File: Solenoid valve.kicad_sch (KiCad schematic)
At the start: 22 parts, among them J1 Conn_01x02, J2 Conn_01x02, J3 Conn_01x02, J4 Conn_01x02, Q1 S8050, Q2 S8050, U1 BTS443P

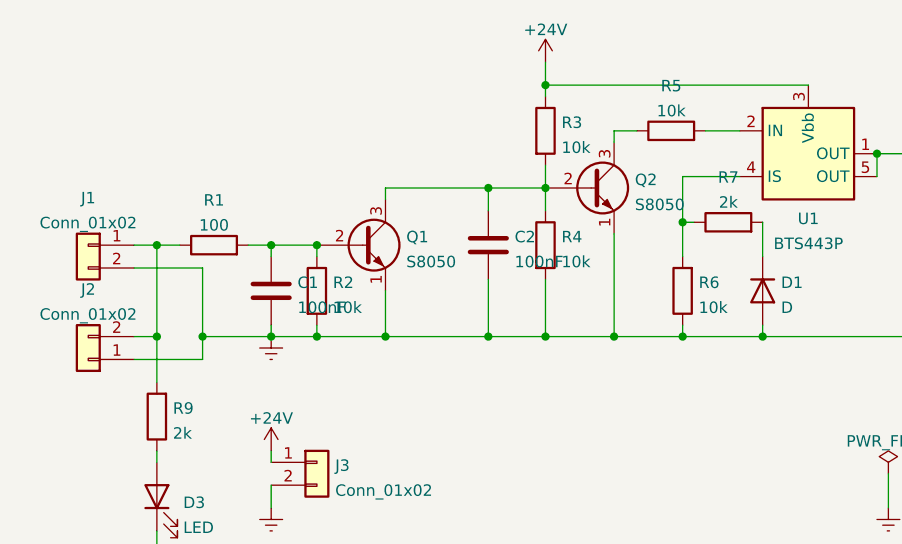
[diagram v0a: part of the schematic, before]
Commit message: Change some routings and S8050's footprint
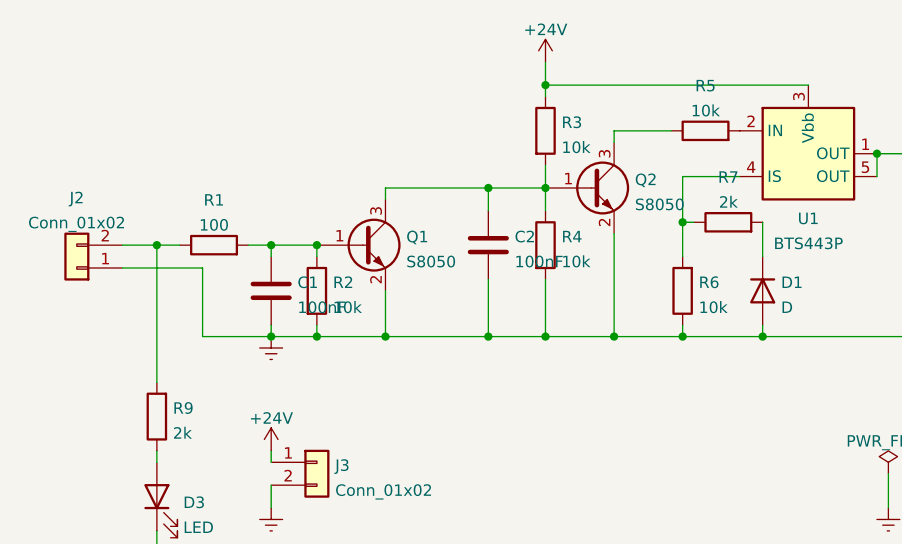
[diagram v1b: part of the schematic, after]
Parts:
- removed J1: Conn_01x02, Connector_AMASS:AMASS_XT30UPB-M_1x02_P5.0mm_Vertical, symbol Connector_Generic:Conn_01x02
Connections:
- net Earth: now also Q1.2 (E), Q2.2 (E); no longer Q1.1 (E), Q2.1 (E)
- net at C1.1, R1.2, R2.1: now also Q1.1 (B); no longer Q1.2 (B)
- net at C2.1, Q1.3 (C), R3.2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: now also Q2.1 (B); no longer Q2.2 (B)
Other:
- moved on the sheet: J2, R5
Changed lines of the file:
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@@
   (junction (at 181.61 66.04) (diameter 0) (color 0 0 0 0)
   )
-  (junction (at 95.25 86.36) (diameter 0) (color 0 0 0 0)
-  )
   (junction (at 133.35 86.36) (diameter 0) (color 0 0 0 0)
   )
@@
   (junction (at 127 86.36) (diameter 0) (color 0 0 0 0)
   )
-  (junction (at 90.17 86.36) (diameter 0) (color 0 0 0 0)
-  )
   (junction (at 102.87 76.2) (diameter 0) (color 0 0 0 0)
   )
@@
     (stroke (width 0) (type default) (color 0 0 0 0))
   )
+  (wire (pts (xy 86.36 76.2) (xy 90.17 76.2))
+    (stroke (width 0) (type default) (color 0 0 0 0))
+  )
   (wire (pts (xy 107.95 86.36) (xy 115.57 86.36))
     (stroke (width 0) (type default) (color 0 0 0 0))
   )
-  (wire (pts (xy 95.25 78.74) (xy 87.63 78.74))
-    (stroke (width 0) (type default) (color 0 0 0 0))
-  )
   (wire (pts (xy 148.59 85.09) (xy 148.59 86.36))
     (stroke (width 0) (type default) (color 0 0 0 0))
@@
     (stroke (width 0) (type default) (color 0 0 0 0))
   )
-  (wire (pts (xy 90.17 86.36) (xy 90.17 76.2))
-    (stroke (width 0) (type default) (color 0 0 0 0))
-  )
-  (wire (pts (xy 87.63 86.36) (xy 90.17 86.36))
-    (stroke (width 0) (type default) (color 0 0 0 0))
-  )
   (wire (pts (xy 176.53 66.04) (xy 181.61 66.04))
     (stroke (width 0) (type default) (color 0 0 0 0))
@@
     (stroke (width 0) (type default) (color 0 0 0 0))
   )
-  (wire (pts (xy 90.17 86.36) (xy 90.17 91.44))
+  (wire (pts (xy 90.17 76.2) (xy 90.17 91.44))
     (stroke (width 0) (type default) (color 0 0 0 0))
   )
@@
     (stroke (width 0) (type default) (color 0 0 0 0))
   )
-  (wire (pts (xy 87.63 76.2) (xy 90.17 76.2))
+  (wire (pts (xy 86.36 78.74) (xy 95.25 78.74))
     (stroke (width 0) (type default) (color 0 0 0 0))
   )
@@
     (stroke (width 0) (type default) (color 0 0 0 0))
   )
-  (wire (pts (xy 95.25 88.9) (xy 95.25 86.36))
-    (stroke (width 0) (type default) (color 0 0 0 0))
-  )
   (wire (pts (xy 102.87 76.2) (xy 107.95 76.2))
     (stroke (width 0) (type default) (color 0 0 0 0))
@@
     (stroke (width 0) (type default) (color 0 0 0 0))
   )
+  (wire (pts (xy 148.59 73.66) (xy 148.59 77.47))
+    (stroke (width 0) (type default) (color 0 0 0 0))
+  )
+  (wire (pts (xy 148.59 68.58) (xy 148.59 73.66))
+    (stroke (width 0) (type default) (color 0 0 0 0))
+  )
+  (wire (pts (xy 148.59 86.36) (xy 157.48 86.36))
+    (stroke (width 0) (type default) (color 0 0 0 0))
+  )
+  (wire (pts (xy 140.97 64.77) (xy 140.97 63.5))
+    (stroke (width 0) (type default) (color 0 0 0 0))
+  )
+  (wire (pts (xy 115.57 86.36) (xy 115.57 81.28))
+    (stroke (width 0) (type default) (color 0 0 0 0))
+  )
+  (wire (pts (xy 133.35 58.42) (xy 162.56 58.42))
+    (stroke (width 0) (type default) (color 0 0 0 0))
+  )
+  (wire (pts (xy 181.61 66.04) (xy 185.42 66.04))
+    (stroke (width 0) (type default) (color 0 0 0 0))
+  )
+  (wire (pts (xy 107.95 77.47) (xy 107.95 76.2))
+    (stroke (width 0) (type default) (color 0 0 0 0))
+  )
   (wire (pts (xy 95.25 78.74) (xy 95.25 86.36))
     (stroke (width 0) (type default) (color 0 0 0 0))
   )
-  (wire (pts (xy 148.59 73.66) (xy 148.59 77.47))
-    (stroke (width 0) (type default) (color 0 0 0 0))
-  )
-  (wire (pts (xy 148.59 68.58) (xy 148.59 73.66))
-    (stroke (width 0) (type default) (color 0 0 0 0))
-  )
-  (wire (pts (xy 148.59 86.36) (xy 157.48 86.36))
-    (stroke (width 0) (type default) (color 0 0 0 0))
-  )
-  (wire (pts (xy 140.97 64.77) (xy 140.97 63.5))
-    (stroke (width 0) (type default) (color 0 0 0 0))
-  )
-  (wire (pts (xy 151.13 63.5) (xy 154.94 63.5))
-    (stroke (width 0) (type default) (color 0 0 0 0))
-  )
-  (wire (pts (xy 115.57 86.36) (xy 115.57 81.28))
-    (stroke (width 0) (type default) (color 0 0 0 0))
-  )
-  (wire (pts (xy 133.35 58.42) (xy 162.56 58.42))
-    (stroke (width 0) (type default) (color 0 0 0 0))
-  )
-  (wire (pts (xy 181.61 66.04) (xy 185.42 66.04))
-    (stroke (width 0) (type default) (color 0 0 0 0))
-  )
-  (wire (pts (xy 107.95 77.47) (xy 107.95 76.2))
-    (stroke (width 0) (type default) (color 0 0 0 0))
-  )
   (wire (pts (xy 157.48 85.09) (xy 157.48 86.36))
     (stroke (width 0) (type default) (color 0 0 0 0))
@@
     (stroke (width 0) (type default) (color 0 0 0 0))
   )
-  (wire (pts (xy 140.97 63.5) (xy 143.51 63.5))
-    (stroke (width 0) (type default) (color 0 0 0 0))
-  )
-  (wire (pts (xy 87.63 88.9) (xy 95.25 88.9))
+  (wire (pts (xy 140.97 63.5) (xy 147.32 63.5))
     (stroke (width 0) (type default) (color 0 0 0 0))
   )
@@
     (pin "1")
   )
-  (symbol (lib_id "Transistor_BJT:S8050") (at 113.03 76.2 0) (unit 1)
+  (symbol (lib_name "S8050_1") (lib_id "Transistor_BJT:S8050") (at 113.03 76.2 0) (unit 1)
     (in_bom yes) (on_board yes) (fields_autoplaced)
     (property "Reference" "Q1" (id 0) (at 117.8814 75.2915 0)
@@
     (pin "2")
   )
-  (symbol (lib_id "Device:R") (at 147.32 63.5 90) (unit 1)
-    (in_bom yes) (on_board yes) (fields_autoplaced)
-    (property "Reference" "R5" (id 0) (at 147.32 58.5175 90))
-    (property "Value" "10k" (id 1) (at 147.32 61.2926 90))
-    (property "Footprint" "Resistor_SMD:R_0603_1608Metric_Pad0.98x0.95mm_HandSolder" (id 2) (at 147.32 65.278 90)
-      (effects (font (size 1.27 1.27)) hide)
-    )
-    (property "Datasheet" "~" (id 3) (at 147.32 63.5 0)
+  (symbol (lib_id "Device:R") (at 151.13 63.5 90) (unit 1)
+    (in_bom yes) (on_board yes) (fields_autoplaced)
+    (property "Reference" "R5" (id 0) (at 151.13 58.5175 90))
+    (property "Value" "10k" (id 1) (at 151.13 61.2926 90))
+    (property "Footprint" "Resistor_SMD:R_0603_1608Metric_Pad0.98x0.95mm_HandSolder" (id 2) (at 151.13 65.278 90)
+      (effects (font (size 1.27 1.27)) hide)
+    )
+    (property "Datasheet" "~" (id 3) (at 151.13 63.5 0)
       (effects (font (size 1.27 1.27)) hide)
     )
@@
     (pin "2")
   )
-  (symbol (lib_id "Connector_Generic:Conn_01x02") (at 82.55 88.9 180) (unit 1)
-    (in_bom yes) (on_board yes) (fields_autoplaced)
-    (property "Reference" "J2" (id 0) (at 82.55 81.1235 0))
-    (property "Value" "Conn_01x02" (id 1) (at 82.55 83.8986 0))
-    (property "Footprint" "Connector_JST:JST_GH_SM02B-GHS-TB_1x02-1MP_P1.25mm_Horizontal" (id 2) (at 82.55 88.9 0)
-      (effects (font (size 1.27 1.27)) hide)
-    )
-    (property "Datasheet" "~" (id 3) (at 82.55 88.9 0)
+  (symbol (lib_id "Connector_Generic:Conn_01x02") (at 81.28 78.74 180) (unit 1)
+    (in_bom yes) (on_board yes) (fields_autoplaced)
+    (property "Reference" "J2" (id 0) (at 81.28 70.9635 0))
+    (property "Value" "Conn_01x02" (id 1) (at 81.28 73.7386 0))
+    (property "Footprint" "Connector_JST:JST_GH_SM02B-GHS-TB_1x02-1MP_P1.25mm_Horizontal" (id 2) (at 81.28 78.74 0)
+      (effects (font (size 1.27 1.27)) hide)
+    )
+    (property "Datasheet" "~" (id 3) (at 81.28 78.74 0)
       (effects (font (size 1.27 1.27)) hide)
     )
@@
     )
     (pin "1")
-  )
-  (symbol (lib_id "Connector_Generic:Conn_01x02") (at 82.55 76.2 0) (mirror y) (unit 1)
-    (in_bom yes) (on_board yes) (fields_autoplaced)
-    (property "Reference" "J1" (id 0) (at 82.55 70.9635 0))
-    (property "Value" "Conn_01x02" (id 1) (at 82.55 73.7386 0))
-    (property "Footprint" "Connector_AMASS:AMASS_XT30UPB-M_1x02_P5.0mm_Vertical" (id 2) (at 82.55 76.2 0)
-      (effects (font (size 1.27 1.27)) hide)
-    )
-    (property "Datasheet" "~" (id 3) (at 82.55 76.2 0)
-      (effects (font (size 1.27 1.27)) hide)
-    )
-    (pin "1")
-    (pin "2")
   )
   (symbol (lib_id "Device:R") (at 133.35 76.2 0) (unit 1)
@@
       (reference "D3") (unit 1) (value "LED") (footprint "LED_SMD:LED_0603_1608Metric_Pad1.05x0.95mm_HandSolder")
     )
-    (path "/e8f47a4f-10df-4ece-90ac-35523bb7b6f5"
-      (reference "J1") (unit 1) (value "Conn_01x02") (footprint "Connector_AMASS:AMASS_XT30UPB-M_1x02_P5.0mm_Vertical")
-    )
     (path "/bc6fce76-cd5f-4a02-afb0-06d97d829d77"

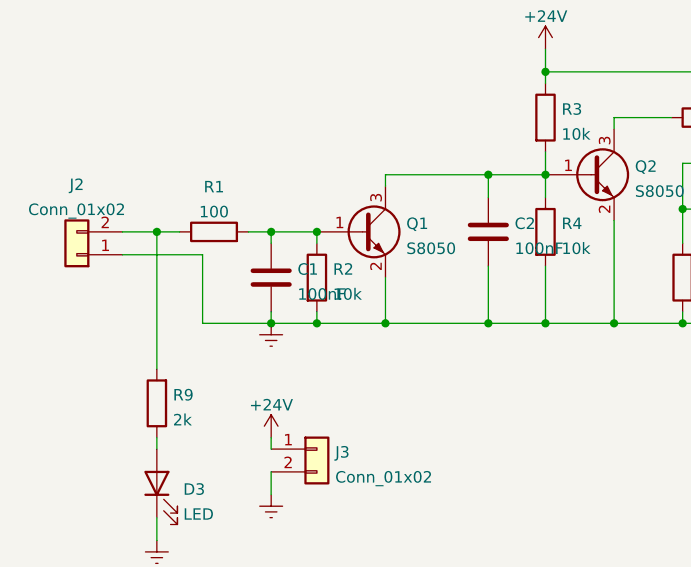
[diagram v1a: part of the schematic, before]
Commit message: Change somes' positions and add mask
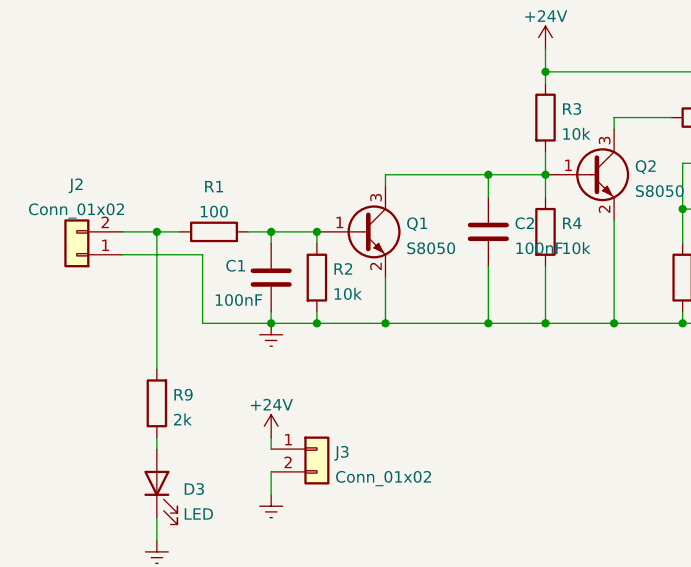
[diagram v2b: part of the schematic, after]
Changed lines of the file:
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@@
   )
   (symbol (lib_id "Device:C") (at 102.87 81.28 0) (unit 1)
-    (in_bom yes) (on_board yes) (fields_autoplaced)
-    (property "Reference" "C1" (id 0) (at 105.791 80.3715 0)
+    (in_bom yes) (on_board yes)
+    (property "Reference" "C1" (id 0) (at 97.79 80.01 0)
       (effects (font (size 1.27 1.27)) (justify left))
     )
-    (property "Value" "100nF" (id 1) (at 105.791 83.1466 0)
+    (property "Value" "100nF" (id 1) (at 96.52 83.82 0)
       (effects (font (size 1.27 1.27)) (justify left))
     )

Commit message: Adjustment for full version
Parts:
- removed C1, C2, C3: 100nF, Capacitor_SMD:C_0603_1608Metric_Pad1.08x0.95mm_HandSolder, symbol Device:C
- removed D1: D, Diode_SMD:D_SOD-123, symbol Device:D
- removed D2, D3: LED, LED_SMD:LED_0603_1608Metric_Pad1.05x0.95mm_HandSolder, symbol Device:LED
- removed J2: Conn_01x02, Connector_JST:JST_GH_SM02B-GHS-TB_1x02-1MP_P1.25mm_Horizontal, symbol Connector_Generic:Conn_01x02
- removed Q1, Q2: S8050, Package_TO_SOT_SMD:SOT-23, symbol Transistor_BJT:S8050
- removed R2, R3, R4, R5, R6, R8: 10k, Resistor_SMD:R_0603_1608Metric_Pad0.98x0.95mm_HandSolder, symbol Device:R
- removed R7, R9: 2k, Resistor_SMD:R_0603_1608Metric_Pad0.98x0.95mm_HandSolder, symbol Device:R
- removed U1: BTS443P, Package_TO_SOT_SMD:TO-252-4, symbol Power_Management:BTS443P
- added C1, C2: 100n, Capacitor_SMD:C_0603_1608Metric, symbol Basic_passive_components:Capacitor
- added D1: LED, Diode_SMD:D_0603_1608Metric, symbol Device:LED
- added J1: Conn_01x02, Connector_JST:JST_GH_SM02B-GHS-TB_1x02-1MP_P1.25mm_Horizontal, symbol Connector_Generic:Conn_01x02
- added Q1: 8050, Package_TO_SOT_SMD:SOT-23, symbol Basic_semiconductor:BJT_NPN
- added Q2: CSD18540Q5B, Package_TO_SOT_SMD:TDSON-8-1, symbol Transistor_FET:CSD18540Q5B
- added R10: 9K, Resistor_SMD:R_0603_1608Metric, symbol Basic_passive_components:Resistor
- added R11: 1K, Resistor_SMD:R_0603_1608Metric, symbol Device:R
- added R2, R5: 10K, Resistor_SMD:R_0603_1608Metric, symbol Basic_passive_components:Resistor
- added R4: 47K, Resistor_SMD:R_0603_1608Metric, symbol Basic_passive_components:Resistor
- added R6: 14K, Resistor_SMD:R_0603_1608Metric, symbol Basic_passive_components:Resistor
- added R7: 38.3K, Resistor_SMD:R_0603_1608Metric, symbol Basic_passive_components:Resistor
- added R8: 200K, Resistor_SMD:R_0603_1608Metric, symbol Basic_passive_components:Resistor
- added R9: 100K, Resistor_SMD:R_0603_1608Metric, symbol Basic_passive_components:Resistor
- added U1: EL357N, Package_SO:SOIC-4_4.55x3.7mm_P2.54mm, symbol Isolator:FODM217C
- added U2: LM5060, Package_SO:VSSOP-10_3x3mm_P0.5mm, symbol Integrated-circuit_transistor_driver:LM5060
- R1: value 100 -> 10K; footprint Resistor_SMD:R_0603_1608Metric_Pad0.98x0.95mm_HandSolder -> Resistor_SMD:R_0603_1608Metric
- renumbered J4 to J2
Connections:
- net +24V: now also R1.2, Q2.5 (D), R10.1, R4.2, R8.2, R9.1, U2.2 (Vin)
- net Earth: no longer J2.2 (Pin_2), J3.2 (Pin_2)
- net at R1.1: now also R2.1, U1.4
- net at J2.1 (Pin_1): now also Q2.1 (S), Q2.2 (S), Q2.3 (S), R11.2, U2.9 (OUT)
- new net: J1.1 (Pin_1), U1.2
- new net: J1.2 (Pin_2), U1.1
- new net: Q2.4 (G), U2.10 (GATE)
- new net: R10.2, U2.1 (SENSE)
- new net: R6.2, R7.2, U2.3 (OVP)
- new net: R7.1, R8.1, U2.4 (UVLO)
- new net: Q1.3 (Collector), R4.1, R5.1, U2.5 (EN)
- new net: C2.2, U2.7 (TIMER)
- new net: R9.2, U2.8 (nPGD)
- new net: D1.2 (A), R11.1
- new net: C1.2, Q1.1 (Base), R2.2
- new net GND: C1.1, C2.1, D1.1 (K), J2.2 (Pin_2), J3.2 (Pin_2), Q1.2 (Emitter), R5.2, R6.1, U1.3, U2.6 (GND)
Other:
- moved on the sheet: J2

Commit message: Add protectionfor EN
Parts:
- removed C1, C2: 100n, Capacitor_SMD:C_0603_1608Metric, symbol Basic_passive_components:Capacitor
- removed R10: 9K, Resistor_SMD:R_0603_1608Metric, symbol Basic_passive_components:Resistor
- removed R2, R5: 10K, Resistor_SMD:R_0603_1608Metric, symbol Basic_passive_components:Resistor
- removed R4: 47K, Resistor_SMD:R_0603_1608Metric, symbol Basic_passive_components:Resistor
- removed R6: 14K, Resistor_SMD:R_0603_1608Metric, symbol Basic_passive_components:Resistor
- removed R7: 38.3K, Resistor_SMD:R_0603_1608Metric, symbol Basic_passive_components:Resistor
- removed R8: 200K, Resistor_SMD:R_0603_1608Metric, symbol Basic_passive_components:Resistor
- removed R9: 100K, Resistor_SMD:R_0603_1608Metric, symbol Basic_passive_components:Resistor
- added C1, C2: 100n, Capacitor_SMD:C_0603_1608Metric, symbol Device:C
- added H1, H2: MountingHole, MountingHole:MountingHole_2.7mm_M2.5, symbol Mechanical:MountingHole
- added R10: 9K, Resistor_SMD:R_0603_1608Metric, symbol Device:R
- added R12: 1K, Resistor_SMD:R_0603_1608Metric, symbol Device:R
- added R2, R5: 10K, Resistor_SMD:R_0603_1608Metric, symbol Device:R
- added R4: 47K, Resistor_SMD:R_0603_1608Metric, symbol Device:R
- added R6: 14K, Resistor_SMD:R_0603_1608Metric, symbol Device:R
- added R7: 38.3K, Resistor_SMD:R_0603_1608Metric, symbol Device:R
- added R8: 200K, Resistor_SMD:R_0603_1608Metric, symbol Device:R
- added R9: 100K, Resistor_SMD:R_0603_1608Metric, symbol Device:R
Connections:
- net +24V: now also R10.1, R4.2, R8.2, R9.2
- net GND: now also C1.2, C2.2, R5.1, R6.1
- net at J1.2 (Pin_2): now also R12.2; no longer U1.1
- net at R1.1, U1.4: now also R2.2
- net at U2.1 (SENSE): now also R10.2
- net at U2.3 (OVP): now also R6.2, R7.2
- net at U2.4 (UVLO): now also R7.1, R8.1
- net at Q1.3 (Collector), U2.5 (EN): now also R4.1, R5.2
- net at U2.7 (TIMER): now also C2.1
- net at U2.8 (nPGD): now also R9.1
- net at Q1.1 (Base): now also C1.1, R2.1
- new net: R12.1, U1.1
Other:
- moved on the sheet: J1
